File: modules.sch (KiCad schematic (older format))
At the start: 7 parts, among them U1 LD1117V33

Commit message: Fix 3D model scale for some caps.
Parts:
- C1: footprint Capacitors_THT:CP_Radial_D4.0mm_P1.50mm -> blubaru:CP_Radial_D4.0mm_P1.50mm
- C2: footprint Capacitors_THT:CP_Radial_D4.0mm_P1.50mm -> blubaru:CP_Radial_D6.3mm_P2.50mm
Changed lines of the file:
@@
 F 0 "C1" H 3325 3950 50  0000 L CNN
 F 1 "10uF" H 3325 3750 50  0000 L CNN
-F 2 "Capacitors_THT:CP_Radial_D4.0mm_P1.50mm" H 3338 3700 50  0001 C CNN
+F 2 "blubaru:CP_Radial_D4.0mm_P1.50mm" H 3338 3700 50  0001 C CNN
 F 3 "http://www.nichicon.co.jp/english/products/pdfs/e-usw.pdf" H 3300 3850 50  0001 C CNN
 	1    3300 3850
@@
 F 0 "C2" H 4225 3950 50  0000 L CNN
 F 1 "100uF" H 4225 3750 50  0000 L CNN
-F 2 "Capacitors_THT:CP_Radial_D4.0mm_P1.50mm" H 4238 3700 50  0001 C CNN
+F 2 "blubaru:CP_Radial_D6.3mm_P2.50mm" H 4238 3700 50  0001 C CNN
 F 3 "http://www.nichicon.co.jp/english/products/pdfs/e-usw.pdf" H 4200 3850 50  0001 C CNN
 	1    4200 3850

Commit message: Fix labels and lay resistors flat.
Left inputs to the line driver were backwards, because the datasheet had
an error. I think I "fixed"it before to match the datasheet.

I also decided to lay the resistors flat. They don't take up that much
room flat, and they will be easier to make pretty on the board, and more
stable with all the vibration.

Also updated the BOM and netlist.
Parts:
- R1, R2: footprint Resistors_THT:R_Axial_DIN0204_L3.6mm_D1.6mm_P1.90mm_Vertical -> Resistors_THT:R_Axial_DIN0204_L3.6mm_D1.6mm_P5.08mm_Horizontal
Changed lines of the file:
@@
 F 0 "R1" V 4480 3650 50  0000 C CNN
 F 1 "750" V 4400 3650 50  0000 C CNN
-F 2 "Resistors_THT:R_Axial_DIN0204_L3.6mm_D1.6mm_P1.90mm_Vertical" V 4330 3650 50  0001 C CNN
+F 2 "Resistors_THT:R_Axial_DIN0204_L3.6mm_D1.6mm_P5.08mm_Horizontal" V 4330 3650 50  0001 C CNN
 F 3 "https://www.seielect.com/Catalog/SEI-CF_CFM.pdf" H 4400 3650 50  0001 C CNN
 	1    4400 3650
@@
 F 0 "R2" V 5230 3650 50  0000 C CNN
 F 1 "330" V 5150 3650 50  0000 C CNN
-F 2 "Resistors_THT:R_Axial_DIN0204_L3.6mm_D1.6mm_P1.90mm_Vertical" V 5080 3650 50  0001 C CNN
+F 2 "Resistors_THT:R_Axial_DIN0204_L3.6mm_D1.6mm_P5.08mm_Horizontal" V 5080 3650 50  0001 C CNN
 F 3 "https://www.seielect.com/Catalog/SEI-CF_CFM.pdf" H 5150 3650 50  0001 C CNN
 	1    5150 3650

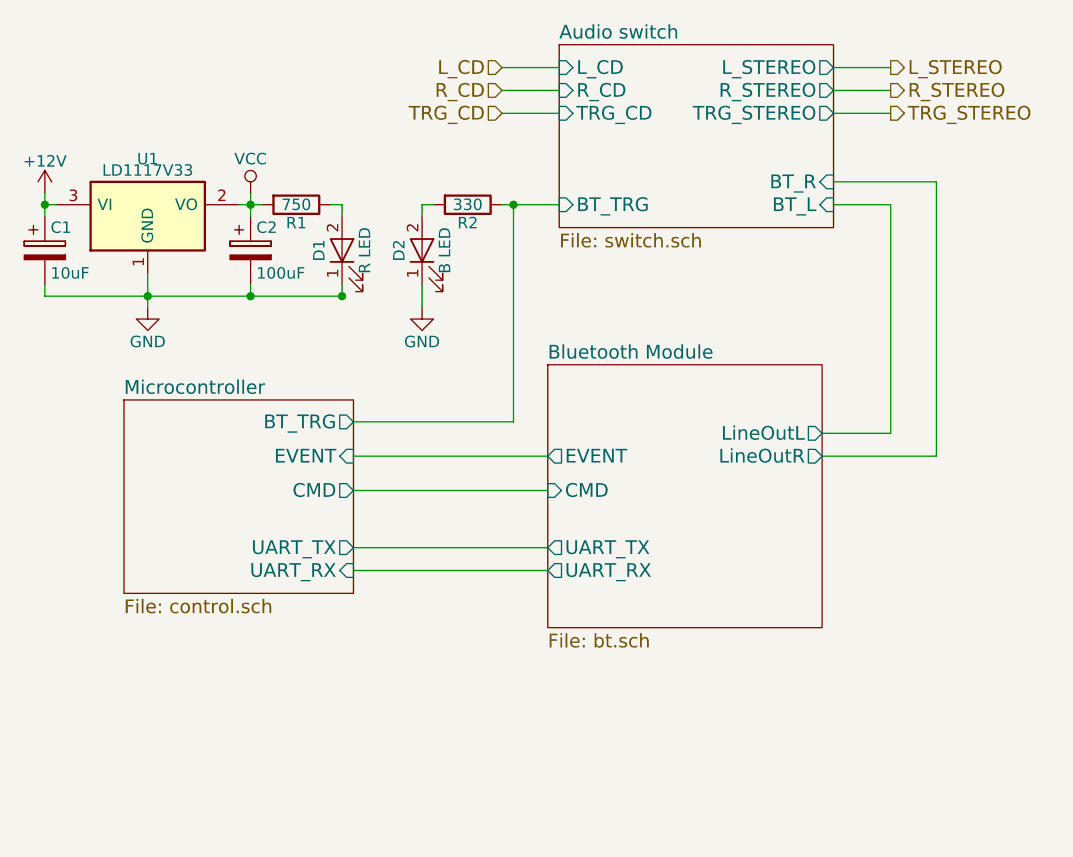
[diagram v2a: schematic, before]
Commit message: Add a line in module and use a smaller jack.
Lots of changes:
Added a line in. This requires another audio switch, so that's added to
the audio switch module.
Also, since I'm using two jacks, I chose a smaller jack module. This
needed a new footprint, and a new 3d model. The footprint is trickier,
since it really needed slots, which OSH won't guarantee. I've given it a
unique footprint to try to optimize the pad size around the edges of the
pins.
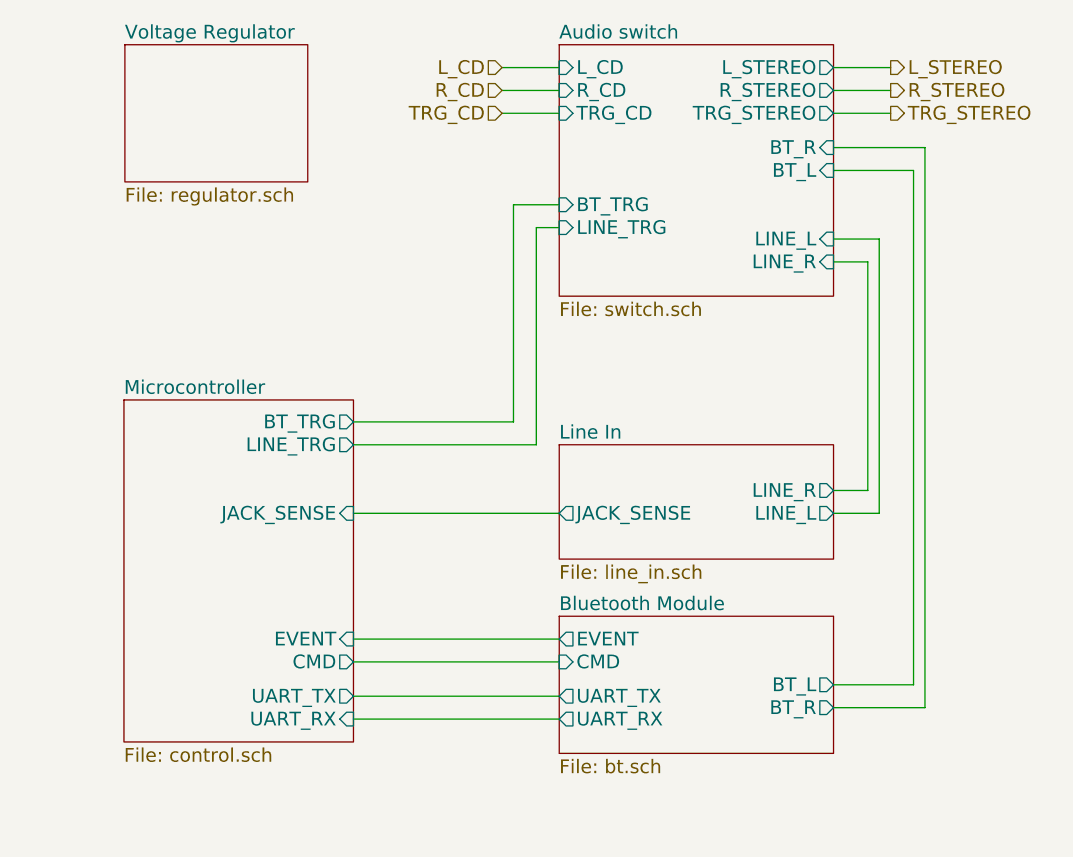
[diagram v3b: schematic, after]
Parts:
- removed C1: 10uF, blubaru:CP_Radial_D4.0mm_P1.50mm, symbol CP
- removed C2: 100uF, blubaru:CP_Radial_D6.3mm_P2.50mm, symbol CP
- removed D1: R LED, LEDs:LED_D3.0mm_Horizontal_O1.27mm_Z2.0mm, symbol LED
- removed D2: B LED, LEDs:LED_D3.0mm_Horizontal_O1.27mm_Z2.0mm, symbol LED
- removed R1: 750, Resistors_THT:R_Axial_DIN0204_L3.6mm_D1.6mm_P5.08mm_Horizontal, symbol R
- removed R2: 330, Resistors_THT:R_Axial_DIN0204_L3.6mm_D1.6mm_P5.08mm_Horizontal, symbol R
- removed U1: LD1117V33, TO_SOT_Packages_THT:TO-220_Vertical, symbol LD1117S33TR
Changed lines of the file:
@@
 $Descr USLetter 11000 8500
 encoding utf-8
-Sheet 3 8
+Sheet 3 10
 Title "Blubaru"
 Date "2017-02-28"
@@
 $EndDescr
 $Sheet
-S 5550 2950 1200 800
+S 5550 2950 1200 1100
 U 58AEC71A
 F0 "Audio switch" 60
@@
 F3 "R_CD" I L 5550 3150 60
 F4 "TRG_CD" I L 5550 3250 60
-F5 "BT_L" I R 6750 3650 60
-F6 "BT_R" I R 6750 3550 60
+F5 "BT_L" I R 6750 3500 60
+F6 "BT_R" I R 6750 3400 60
 F7 "BT_TRG" I L 5550 3650 60
 F8 "L_STEREO" O R 6750 3050 60
 F9 "R_STEREO" O R 6750 3150 60
 F10 "TRG_STEREO" O R 6750 3250 60
+F11 "LINE_TRG" I L 5550 3750 60
+F12 "LINE_R" I R 6750 3900 60
+F13 "LINE_L" I R 6750 3800 60
 $EndSheet
 Wire Wire Line
@@
 TRG_STEREO
 $Sheet
-S 3646 4504 1004 846
+S 3646 4504 1004 1496
 U 58B171C6
 F0 "Microcontroller" 60
 F1 "control.sch" 60
-F2 "UART_TX" O R 4650 5150 60
-F3 "UART_RX" I R 4650 5250 60
-F4 "CMD" O R 4650 4900 60
-F5 "EVENT" I R 4650 4750 60
+F2 "UART_TX" O R 4650 5800 60
+F3 "UART_RX" I R 4650 5900 60
+F4 "CMD" O R 4650 5650 60
+F5 "EVENT" I R 4650 5550 60
 F6 "BT_TRG" O R 4650 4600 60
+F7 "LINE_TRG" O R 4650 4700 60
+F8 "JACK_SENSE" I R 4650 5000 60
 $EndSheet
 $Sheet
-S 5500 4350 1200 1150
+S 5550 5450 1200 600
 U 58B189CE
 F0 "Bluetooth Module" 60
 F1 "bt.sch" 60
-F2 "LineOutL" O R 6700 4650 60
-F3 "LineOutR" O R 6700 4750 60
-F4 "UART_TX" O L 5500 5150 60
-F5 "UART_RX" O L 5500 5250 60
-F6 "CMD" I L 5500 4900 60
-F7 "EVENT" O L 5500 4750 60
+F2 "BT_L" O R 6750 5750 60
+F3 "BT_R" O R 6750 5850 60
+F4 "UART_TX" O L 5550 5800 60
+F5 "UART_RX" O L 5550 5900 60
+F6 "CMD" I L 5550 5650 60
+F7 "EVENT" O L 5550 5550 60
 $EndSheet
-Wire Wire Line
-	4650 5150 5500 5150
-Wire Wire Line
-	4650 5250 5500 5250
-Wire Wire Line
-	4650 4750 5500 4750
-Wire Wire Line
-	6750 3650 7000 3650
-Wire Wire Line
-	7000 3650 7000 4650
-Wire Wire Line
-	7000 4650 6700 4650
-Wire Wire Line
-	6750 3550 7200 3550
-Wire Wire Line
-	7200 3550 7200 4750
-Wire Wire Line
-	7200 4750 6700 4750
 Wire Wire Line
 	4650 4600 5350 4600
 Wire Wire Line
 	5350 4600 5350 3650
-Wire Wire Line
-	5300 3650 5550 3650
 Text HLabel 5300 3250 0    60   Input ~ 0
 TRG_CD
 Wire Wire Line
-	4650 4900 5500 4900
-$Comp
-L GND #PWR07
-U 1 1 59484363
-P 3750 4100
-F 0 "#PWR07" H 3750 3850 50  0001 C CNN
-F 1 "GND" H 3750 3950 50  0000 C CNN
-F 2 "" H 3750 4100 50  0001 C CNN
-F 3 "" H 3750 4100 50  0001 C CNN
-	1    3750 4100
-	1    0    0    -1
-$EndComp
+	5550 5550 4650 5550
 Wire Wire Line
-	3750 3950 3750 4100
-$Comp
-L +12V #PWR08
-U 1 1 59484575
-P 3300 3600
-F 0 "#PWR08" H 3300 3450 50  0001 C CNN
-F 1 "+12V" H 3300 3740 50  0000 C CNN
-F 2 "" H 3300 3600 50  0001 C CNN
-F 3 "" H 3300 3600 50  0001 C CNN
-	1    3300 3600
-	1    0    0    -1
-$EndComp
+	4650 5650 5550 5650
 Wire Wire Line
-	3300 3600 3300 3700
+	5550 5800 4650 5800
 Wire Wire Line
-	4200 3600 4200 3700
-$Comp
-L CP C1
-U 1 1 59484D99
-P 3300 3850
-F 0 "C1" H 3325 3950 50  0000 L CNN
-F 1 "10uF" H 3325 3750 50  0000 L CNN
-F 2 "blubaru:CP_Radial_D4.0mm_P1.50mm" H 3338 3700 50  0001 C CNN
-F 3 "http://www.nichicon.co.jp/english/products/pdfs/e-usw.pdf" H 3300 3850 50  0001 C CNN
-	1    3300 3850
-	1    0    0    -1
-$EndComp
-$Comp
-L CP C2
-U 1 1 59484E96
-P 4200 3850
-F 0 "C2" H 4225 3950 50  0000 L CNN
-F 1 "100uF" H 4225 3750 50  0000 L CNN
-F 2 "blubaru:CP_Radial_D6.3mm_P2.50mm" H 4238 3700 50  0001 C CNN
-F 3 "http://www.nichicon.co.jp/english/products/pdfs/e-usw.pdf" H 4200 3850 50  0001 C CNN
-	1    4200 3850
-	1    0    0    -1
-$EndComp
+	4650 5900 5550 5900
 Wire Wire Line
-	3300 4000 3300 4050
-Connection ~ 3750 4050
+	4650 4700 5450 4700
 Wire Wire Line
-	4200 4050 4200 4000
-Connection ~ 4200 3650
-Connection ~ 3300 3650
-$Comp
-L VCC #PWR09
-U 1 1 59486886
-P 4200 3600
-F 0 "#PWR09" H 4200 3450 50  0001 C CNN
-F 1 "VCC" H 4200 3750 50  0000 C CNN
-F 2 "" H 4200 3600 50  0001 C CNN
-F 3 "" H 4200 3600 50  0001 C CNN
-	1    4200 3600
-	1    0    0    -1
-$EndComp
-$Comp
-L LD1117S33TR U1
-U 1 1 5949FB36
-P 3750 3700
-F 0 "U1" H 3750 3950 50  0000 C CNN
-F 1 "LD1117V33" H 3750 3900 50  0000 C CNN
-F 2 "TO_SOT_Packages_THT:TO-220_Vertical" H 3750 3800 50  0001 C CNN
-F 3 "http://www.st.com/content/ccc/resource/technical/document/datasheet/99/3b/7d/91/91/51/4b/be/CD00000544.pdf/files/CD00000544.pdf/jcr:content/translations/en.CD00000544.pdf" H 3750 3700 50  0001 C CNN
-	1    3750 3700
-	1    0    0    -1
-$EndComp
+	5450 4700 5450 3750
 Wire Wire Line
-	3350 3650 3300 3650
+	5450 3750 5550 3750
 Wire Wire Line
-	4150 3650 4250 3650
-$Comp
-L R R1
-U 1 1 594DE951
-P 4400 3650
-F 0 "R1" V 4480 3650 50  0000 C CNN
-F 1 "750" V 4400 3650 50  0000 C CNN
-F 2 "Resistors_THT:R_Axial_DIN0204_L3.6mm_D1.6mm_P5.08mm_Horizontal" V 4330 3650 50  0001 C CNN
-F 3 "https://www.seielect.com/Catalog/SEI-CF_CFM.pdf" H 4400 3650 50  0001 C CNN
-	1    4400 3650
-	0    1    1    0
-$EndComp
-$Comp
-L LED D1
-U 1 1 594DE9F6
-P 4600 3850
-F 0 "D1" H 4600 3950 50  0000 C CNN
-F 1 "R LED" H 4600 3750 50  0000 C CNN
-F 2 "LEDs:LED_D3.0mm_Horizontal_O1.27mm_Z2.0mm" H 4600 3850 50  0001 C CNN
-F 3 "http://www.kingbrightusa.com/images/catalog/SPEC/WP710A10LSECK-J3.pdf" H 4600 3850 50  0001 C CNN
-	1    4600 3850
-	0    -1   -1   0
-$EndComp
+	5550 5000 4650 5000
 Wire Wire Line
-	4550 3650 4600 3650
+	6750 3900 6900 3900
 Wire Wire Line
-	4600 3650 4600 3700
+	6900 3900 6900 4900
 Wire Wire Line
-	4600 4050 4600 4000
-Connection ~ 4200 4050
-$Comp
-L R R2
-U 1 1 594DF732
-P 5150 3650
-F 0 "R2" V 5230 3650 50  0000 C CNN
-F 1 "330" V 5150 3650 50  0000 C CNN
-F 2 "Resistors_THT:R_Axial_DIN0204_L3.6mm_D1.6mm_P5.08mm_Horizontal" V 5080 3650 50  0001 C CNN
-F 3 "https://www.seielect.com/Catalog/SEI-CF_CFM.pdf" H 5150 3650 50  0001 C CNN
-	1    5150 3650
-	0    1    1    0
-$EndComp
-$Comp
-L LED D2
-U 1 1 594DFA15
-P 4950 3850
-F 0 "D2" H 4950 3950 50  0000 C CNN
-F 1 "B LED" H 4950 3750 50  0000 C CNN
-F 2 "LEDs:LED_D3.0mm_Horizontal_O1.27mm_Z2.0mm" H 4950 3850 50  0001 C CNN
-F 3 "http://www.kingbrightusa.com/images/catalog/SPEC/WP710A10LVBC-D.pdf" H 4950 3850 50  0001 C CNN
-	1    4950 3850
-	0    -1   -1   0
-$EndComp
-Connection ~ 5350 3650
+	6900 4900 6750 4900
 Wire Wire Line
-	5000 3650 4950 3650
+	6750 5000 6950 5000
 Wire Wire Line
-	4950 3650 4950 3700
+	6950 5000 6950 3800
 Wire Wire Line
-	4950 4000 4950 4100
-Connection ~ 4600 4050
-$Comp
-L GND #PWR010
-U 1 1 594E013B
-P 4950 4100
-F 0 "#PWR010" H 4950 3850 50  0001 C CNN
-F 1 "GND" H 4950 3950 50  0000 C CNN
-F 2 "" H 4950 4100 50  0001 C CNN
-F 3 "" H 4950 4100 50  0001 C CNN
-	1    4950 4100
-	1    0    0    -1
-$EndComp
+	6950 3800 6750 3800
 Wire Wire Line
-	3300 4050 4600 4050
+	6750 3500 7100 3500
+Wire Wire Line
+	7100 3500 7100 5750
+Wire Wire Line
+	7100 5750 6750 5750
+Wire Wire Line
+	6750 5850 7150 5850
+Wire Wire Line
+	7150 5850 7150 3400
+Wire Wire Line
+	7150 3400 6750 3400
+$Sheet
+S 5550 4700 1200 500
+U 595F0252
+F0 "Line In" 60
+F1 "line_in.sch" 60
+F2 "JACK_SENSE" O L 5550 5000 60
+F3 "LINE_L" O R 6750 5000 60
+F4 "LINE_R" O R 6750 4900 60
+$EndSheet
+$Sheet
+S 3650 2950 800  600
+U 597565F8
+F0 "Voltage Regulator" 60
+F1 "regulator.sch" 60
+$EndSheet
+Wire Wire Line
+	5350 3650 5550 3650
 $EndSCHEMATC

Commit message: Major update to use Atmel ATTINY4313
Replace Pro Micro as microcontroller. Mostly contianed within the
control sheet.
Moved LEDs all onto control sheet.
Updated a few capacitors.
Added a reset switch. Still need to decide part.
Updated a few capacitor models for 4.0.7
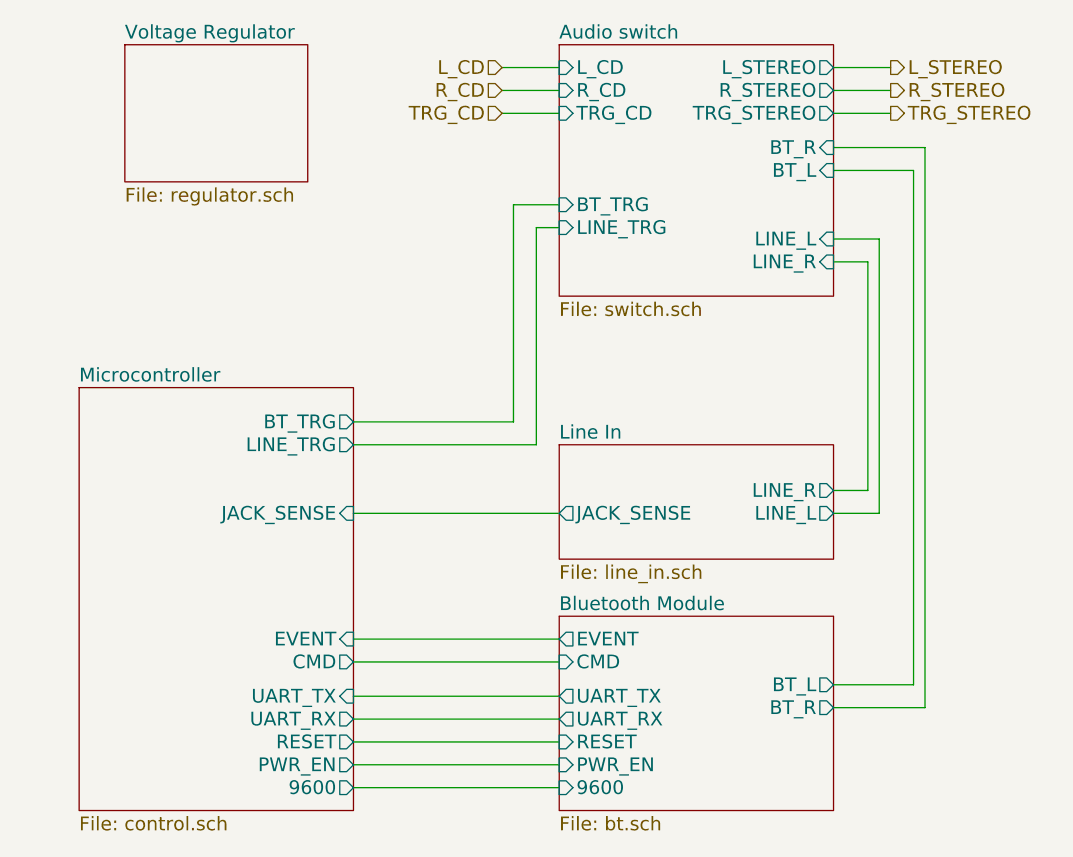
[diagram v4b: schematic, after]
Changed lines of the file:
@@
 TRG_STEREO
 $Sheet
-S 3646 4504 1004 1496
-U 58B171C6
-F0 "Microcontroller" 60
-F1 "control.sch" 60
-F2 "UART_TX" O R 4650 5800 60
-F3 "UART_RX" I R 4650 5900 60
-F4 "CMD" O R 4650 5650 60
-F5 "EVENT" I R 4650 5550 60
-F6 "BT_TRG" O R 4650 4600 60
-F7 "LINE_TRG" O R 4650 4700 60
-F8 "JACK_SENSE" I R 4650 5000 60
-$EndSheet
-$Sheet
-S 5550 5450 1200 600
+S 5550 5450 1200 850
 U 58B189CE
 F0 "Bluetooth Module" 60
@@
 F6 "CMD" I L 5550 5650 60
 F7 "EVENT" O L 5550 5550 60
+F8 "RESET" I L 5550 6000 60
+F9 "9600" I L 5550 6200 60
+F10 "PWR_EN" I L 5550 6100 60
 $EndSheet
 Wire Wire Line
@@
 Wire Wire Line
 	5350 3650 5550 3650
+$Sheet
+S 3450 4450 1200 1850
+U 59F28ACC
+F0 "Microcontroller" 60
+F1 "control.sch" 60
+F2 "UART_TX" I R 4650 5800 60
+F3 "UART_RX" O R 4650 5900 60
+F4 "CMD" O R 4650 5650 60
+F5 "EVENT" I R 4650 5550 60
+F6 "BT_TRG" O R 4650 4600 60
+F7 "LINE_TRG" O R 4650 4700 60
+F8 "JACK_SENSE" I R 4650 5000 60
+F9 "RESET" O R 4650 6000 60
+F10 "PWR_EN" O R 4650 6100 60
+F11 "9600" O R 4650 6200 60
+$EndSheet
+Wire Wire Line
+	4650 6000 5550 6000
+Wire Wire Line
+	4650 6100 5550 6100
+Wire Wire Line
+	4650 6200 5550 6200
 $EndSCHEMATC

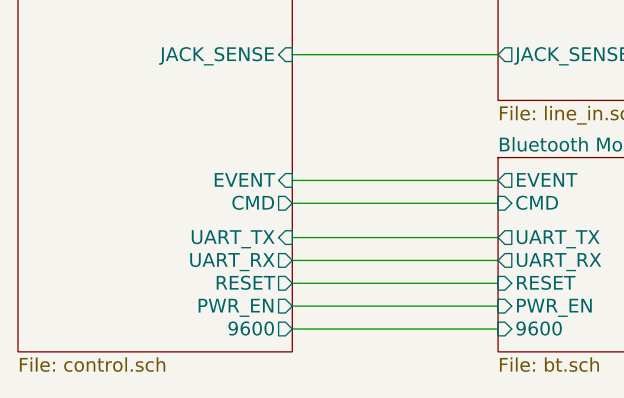
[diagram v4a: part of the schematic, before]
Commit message: Rename the bluetooth reset line
This is needed so it doesn't conflict with the MCU reset line of the
same name. Apparently that puts them on the same net.

Also, reorder the LEDs so they have nicer numbers on the board.
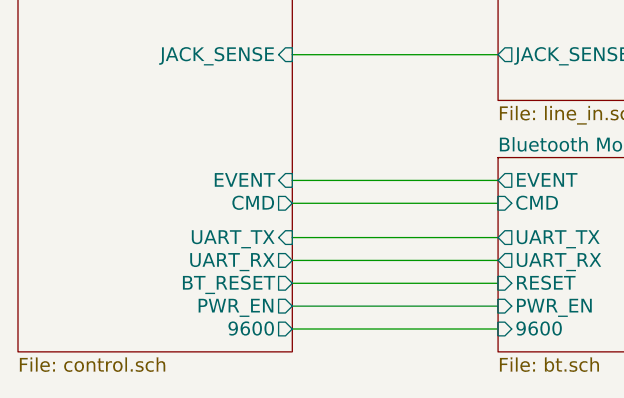
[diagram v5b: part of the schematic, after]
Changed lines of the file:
@@
 F7 "LINE_TRG" O R 4650 4700 60
 F8 "JACK_SENSE" I R 4650 5000 60
-F9 "RESET" O R 4650 6000 60
+F9 "BT_RESET" O R 4650 6000 60
 F10 "PWR_EN" O R 4650 6100 60
 F11 "9600" O R 4650 6200 60
